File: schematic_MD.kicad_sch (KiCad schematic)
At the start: 30 parts, among them J1 XT60, J10 Gate_PWR_Jump, J11 Gate_PWR_Jump, J12 EXPWR_GND, J13 EXPWR_GND, J2 XT60, J3 XT60, J4 CAN_Bus, J5 Rotaly_encoder_1, J6 Rotaly_encoder_2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

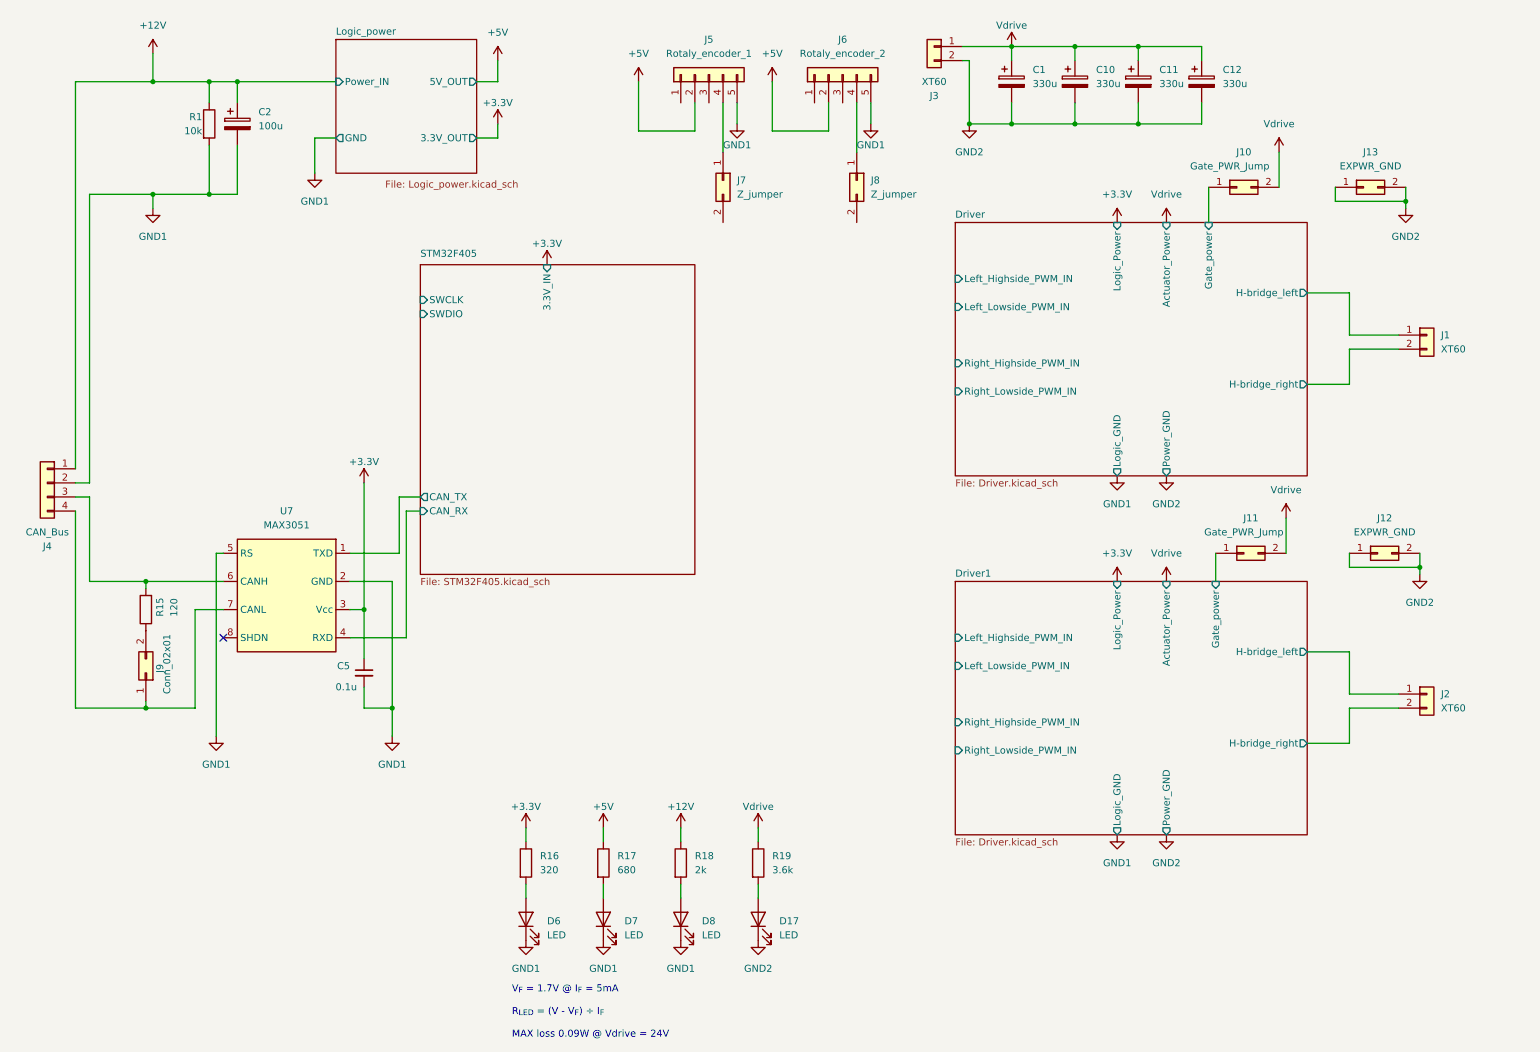
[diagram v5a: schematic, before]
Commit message: Update motor driver circuit
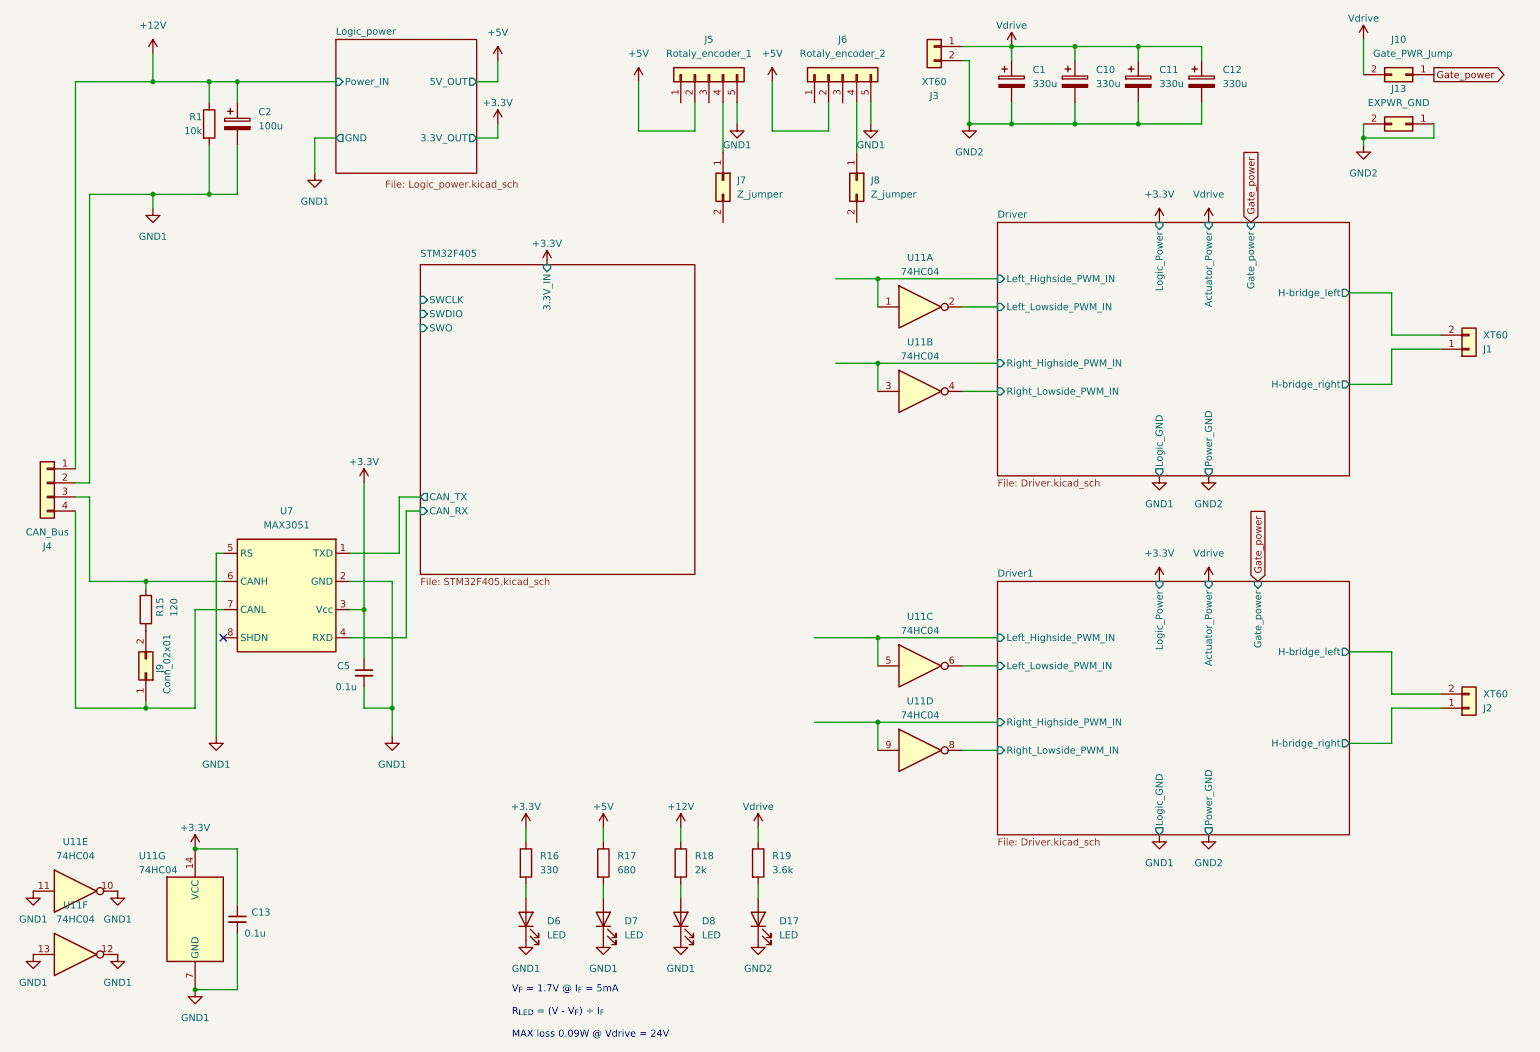
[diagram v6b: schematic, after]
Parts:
- removed J11: Gate_PWR_Jump, Connector_PinHeader_2.54mm:PinHeader_1x02_P2.54mm_Vertical, symbol Connector_Generic:Conn_02x01
- removed J12: EXPWR_GND, Connector_PinHeader_2.54mm:PinHeader_1x02_P2.54mm_Vertical, symbol Connector_Generic:Conn_02x01
- added C13: 0.1u, Capacitor_SMD:C_01005_0402Metric_Pad0.57x0.30mm_HandSolder, symbol Device:C_Small
- added U11: 74HC04, symbol 74xx:74HC04
- C5: footprint (none) -> Capacitor_SMD:C_01005_0402Metric_Pad0.57x0.30mm_HandSolder
- R16: value 320 -> 330; footprint (none) -> Resistor_SMD:R_0603_1608Metric_Pad0.98x0.95mm_HandSolder
- R17, R18, R19: footprint (none) -> Resistor_SMD:R_0603_1608Metric_Pad0.98x0.95mm_HandSolder
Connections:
- net +3.3V: now also C13.1, U11.14 (VCC)
- net Driver/H-bridge_left: now also J1.2 (Pin_2); no longer J1.1 (Pin_1)
- net Driver/H-bridge_right: now also J1.1 (Pin_1); no longer J1.2 (Pin_2)
- net Driver/Left_Highside_PWM_IN: now also U11.1
- net Driver/Left_Lowside_PWM_IN: now also U11.2
- net Driver/Right_Highside_PWM_IN: now also U11.3
- net Driver/Right_Lowside_PWM_IN: now also U11.4
- net Driver1/H-bridge_left: now also J2.2 (Pin_2); no longer J2.1 (Pin_1)
- net Driver1/H-bridge_right: now also J2.1 (Pin_1); no longer J2.2 (Pin_2)
- net Driver1/Left_Highside_PWM_IN: now also U11.5
- net Driver1/Left_Lowside_PWM_IN: now also U11.6
- net Driver1/Right_Highside_PWM_IN: now also U11.9
- net Driver1/Right_Lowside_PWM_IN: now also U11.8
- net GND1: now also C13.2, U11.10, U11.11, U11.12, U11.13, U11.7 (GND)
- net Driver/Gate_power renamed Gate_power
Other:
- sheet STM32F405 ports: added SWO; removed none
- moved on the sheet: J1, J10, J13, J2

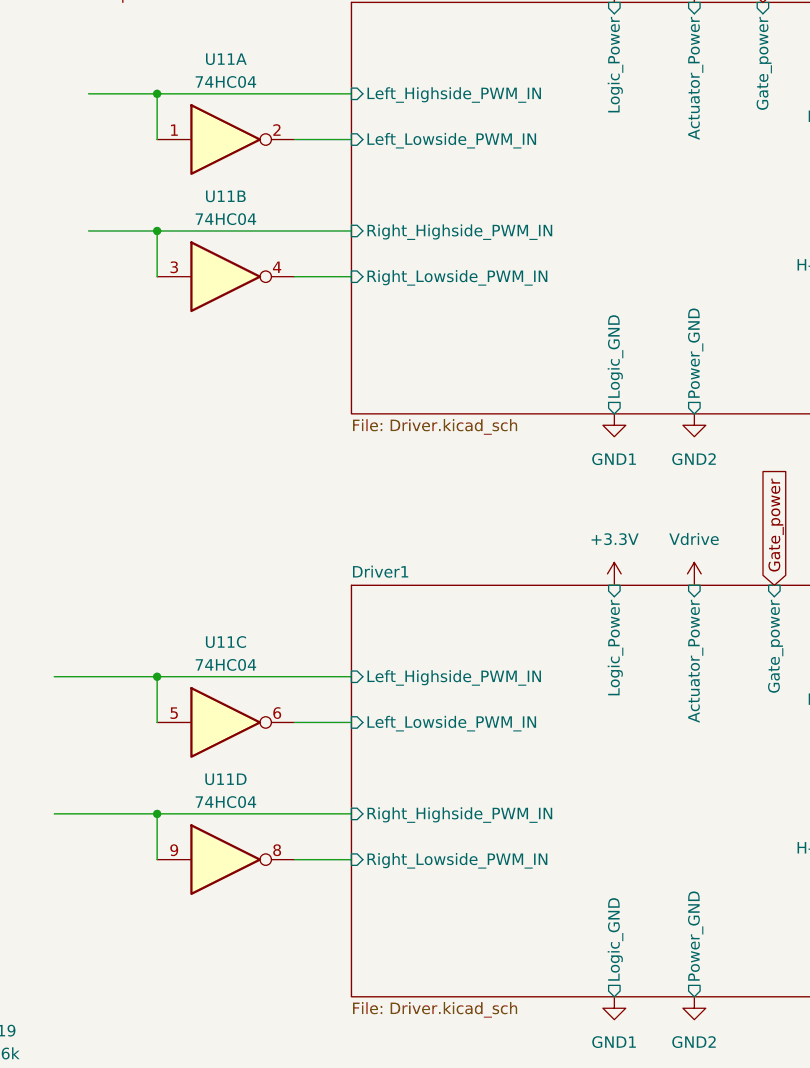
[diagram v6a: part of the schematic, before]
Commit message: Change gate driver
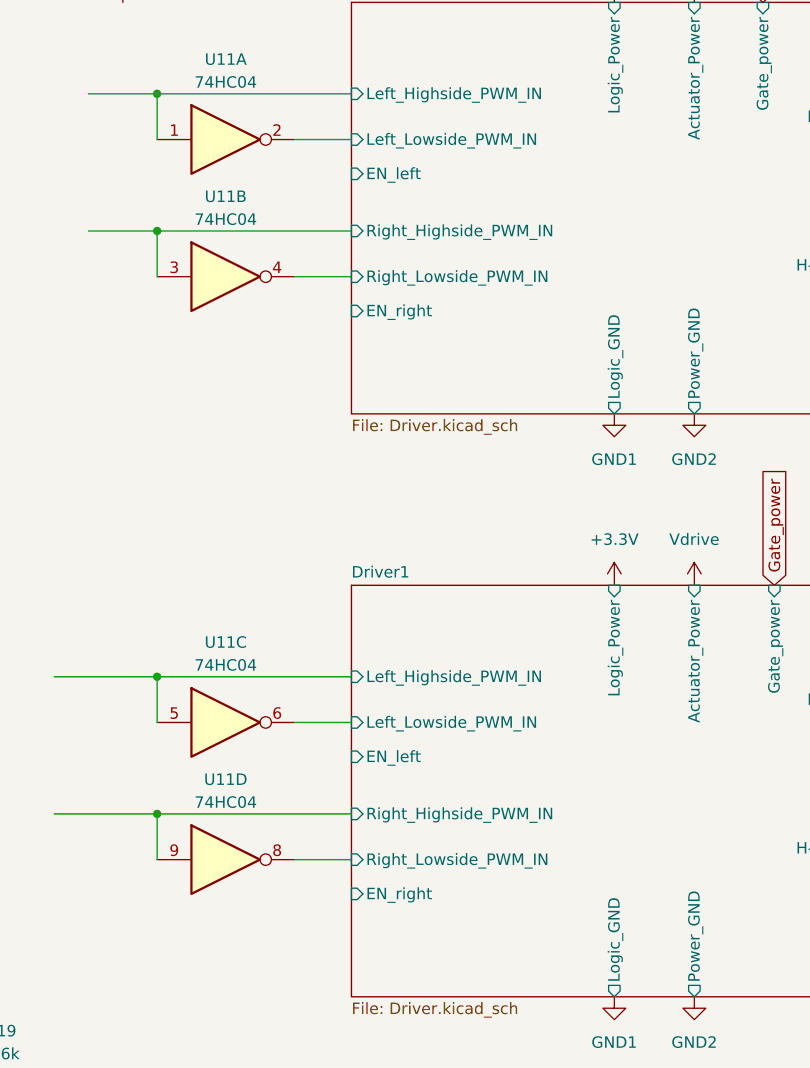
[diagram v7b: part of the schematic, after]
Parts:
- U11: footprint (none) -> Package_SO:SOIC-14_3.9x8.7mm_P1.27mm
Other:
- sheet Driver ports: added EN_left, EN_right; removed none
- sheet Driver1 ports: added EN_left, EN_right; removed none
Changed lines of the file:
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@@
       (effects (font (size 1.27 1.27)))
     )
-    (property "Footprint" "" (at 177.8 80.01 0)
+    (property "Footprint" "Package_SO:SOIC-14_3.9x8.7mm_P1.27mm" (at 177.8 80.01 0)
       (effects (font (size 1.27 1.27)) hide)
     )
@@
       (effects (font (size 1.27 1.27)))
     )
-    (property "Footprint" "" (at 25.4 181.61 0)
+    (property "Footprint" "Package_SO:SOIC-14_3.9x8.7mm_P1.27mm" (at 25.4 181.61 0)
       (effects (font (size 1.27 1.27)) hide)
     )
@@
       (effects (font (size 1.27 1.27)))
     )
-    (property "Footprint" "" (at 177.8 129.54 0)
+    (property "Footprint" "Package_SO:SOIC-14_3.9x8.7mm_P1.27mm" (at 177.8 129.54 0)
       (effects (font (size 1.27 1.27)) hide)
     )
@@
       (effects (font (size 1.27 1.27)))
     )
-    (property "Footprint" "" (at 25.4 170.18 0)
+    (property "Footprint" "Package_SO:SOIC-14_3.9x8.7mm_P1.27mm" (at 25.4 170.18 0)
       (effects (font (size 1.27 1.27)) hide)
     )
@@
       (effects (font (size 1.27 1.27)))
     )
-    (property "Footprint" "" (at 177.8 64.77 0)
+    (property "Footprint" "Package_SO:SOIC-14_3.9x8.7mm_P1.27mm" (at 177.8 64.77 0)
       (effects (font (size 1.27 1.27)) hide)
     )
@@
       (effects (font (size 1.27 1.27)) (justify left))
     )
-    (property "Footprint" "" (at 46.99 175.26 0)
+    (property "Footprint" "Package_SO:SOIC-14_3.9x8.7mm_P1.27mm" (at 46.99 175.26 0)
       (effects (font (size 1.27 1.27)) hide)
     )
@@
       (effects (font (size 1.27 1.27)))
     )
-    (property "Footprint" "" (at 177.8 144.78 0)
+    (property "Footprint" "Package_SO:SOIC-14_3.9x8.7mm_P1.27mm" (at 177.8 144.78 0)
       (effects (font (size 1.27 1.27)) hide)
     )
@@
       (effects (font (size 1.27 1.27)) (justify right))
     )
+    (pin "EN_right" input (at 191.77 83.82 180)
+      (effects (font (size 1.27 1.27)) (justify left))
+    )
+    (pin "EN_left" input (at 191.77 68.58 180)
+      (effects (font (size 1.27 1.27)) (justify left))
+    )
     (instances
       (project "schematic_MD"
@@
       (effects (font (size 1.27 1.27)) (justify right))
     )
-    (instances
+    (pin "EN_right" input (at 191.77 148.59 180)
+      (effects (font (size 1.27 1.27)) (justify left))
+    )
+    (pin "EN_left" input (at 191.77 133.35 180)
+      (effects (font (size 1.27 1.27)) (justify left))
+    )
+    (instances

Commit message: fix drive circuit
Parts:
- added C18: 10u, Capacitor_SMD:C_1210_3225Metric_Pad1.33x2.70mm_HandSolder, symbol Device:C_Small
- added C3: 1uF, Capacitor_SMD:C_0603_1608Metric_Pad1.08x0.95mm_HandSolder, symbol Device:C_Small
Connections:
- net GND2: now also C18.2, C3.2
- net Vdrive: now also C18.1, C3.1
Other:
- moved on the sheet: J10, J13
